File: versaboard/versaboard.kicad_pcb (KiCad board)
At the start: 4 copper layers, 61 x 43 mm, 30 parts, among them J1 UART, J39 Conn_02x20_Odd_Even, J4 DBG, J40 Conn_02x20_Odd_Even, SW1 RST, U1 ATSAML21G18B-AUT, X1 32.768kHz

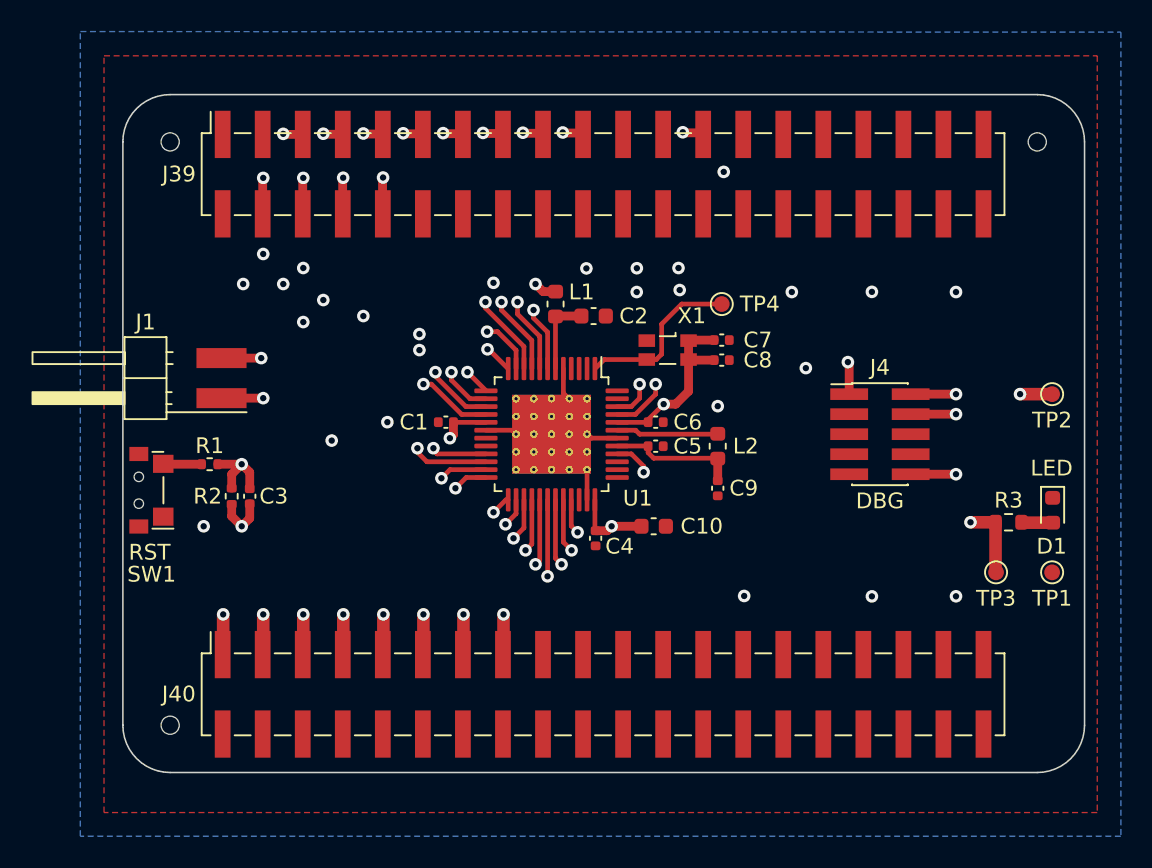
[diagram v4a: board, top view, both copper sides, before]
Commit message: versaboard r0003: avoid FPGA pin bank 1
Pin bank 1 on the ECP5 evaluation board is +2.5V by default and this can
only be changed by resoldering SMD resistors. Yeah, no.
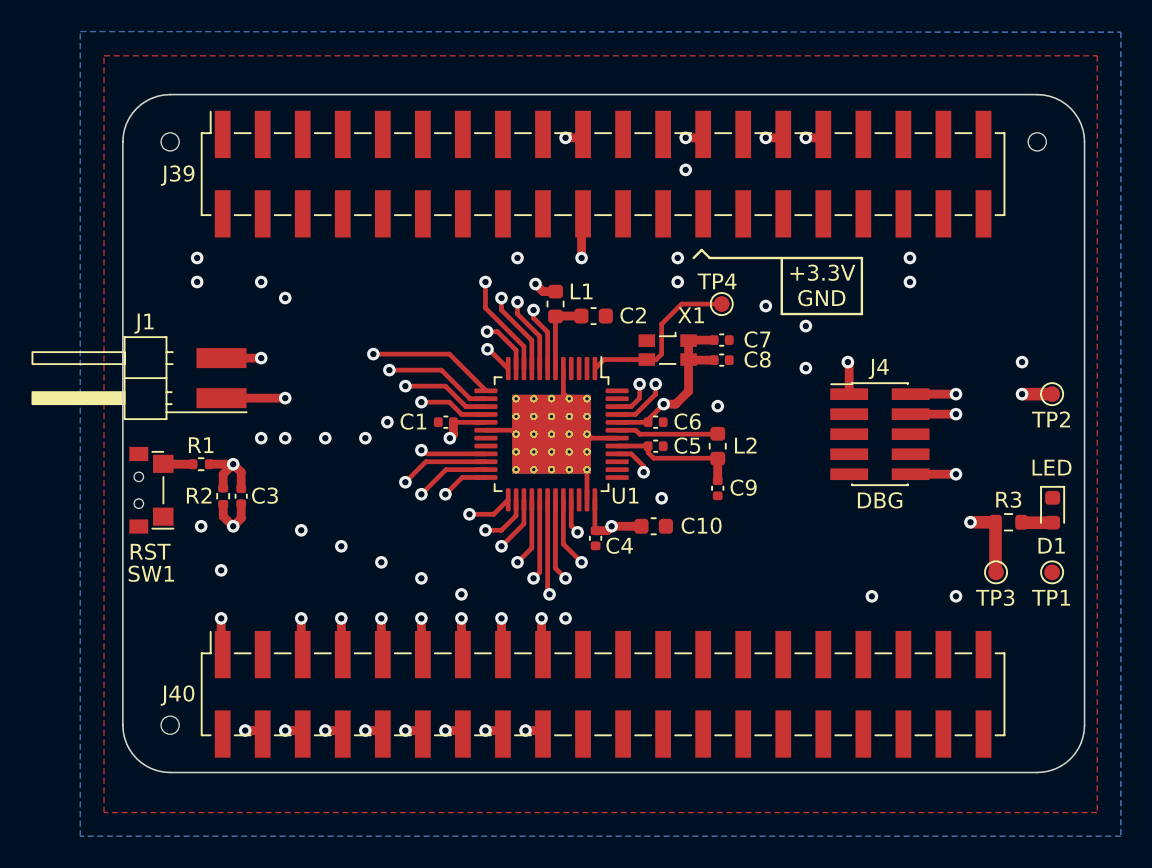
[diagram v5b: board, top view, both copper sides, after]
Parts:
- moved R2 0.54 mm to (36.9, 66.2)
- moved C3 0.54 mm to (38.0, 66.2)
- moved R1 0.54 mm to (35.5, 64.1)
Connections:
- J39 pad 10: /YT -> unconnected-(J39-Pad10)
- J39 pad 11: /NHB3 -> unconnected-(J39-Pad11)
- J39 pad 13: /NHB4 -> unconnected-(J39-Pad13)
- J39 pad 15: /NHB5 -> unconnected-(J39-Pad15)
- J39 pad 17: /NHB6 -> unconnected-(J39-Pad17)
- J39 pad 19: /NHB7 -> /SHB
- J39 pad 20: unconnected-(J39-Pad20) -> /GO
- J39 pad 29: unconnected-(J39-Pad29) -> /MF
- J39 pad 31: unconnected-(J39-Pad31) -> /YT
- J39 pad 4: /SHB -> unconnected-(J39-Pad4)
- J39 pad 5: /NHB0 -> unconnected-(J39-Pad5)
- J39 pad 6: /GO -> unconnected-(J39-Pad6)
- J39 pad 7: /NHB1 -> unconnected-(J39-Pad7)
- J39 pad 8: /MF -> unconnected-(J39-Pad8)
- J39 pad 9: /NHB2 -> unconnected-(J39-Pad9)
- J40 pad 10: unconnected-(J40-Pad10) -> /NHB3
- J40 pad 11: /PB5 -> /PB4
- J40 pad 12: unconnected-(J40-Pad12) -> /NHB4
- J40 pad 13: /PB6 -> /PB5
- J40 pad 14: unconnected-(J40-Pad14) -> /NHB5
- J40 pad 15: /PB7 -> /PB6
- J40 pad 16: unconnected-(J40-Pad16) -> /NHB6
- J40 pad 17: unconnected-(J40-Pad17) -> /PB7
- J40 pad 18: unconnected-(J40-Pad18) -> /NHB7
- J40 pad 3: /PB1 -> unconnected-(J40-Pad3)
- J40 pad 4: unconnected-(J40-Pad4) -> /NHB0
- J40 pad 5: /PB2 -> /PB1
- J40 pad 6: unconnected-(J40-Pad6) -> /NHB1
- J40 pad 7: /PB3 -> /PB2
- J40 pad 8: unconnected-(J40-Pad8) -> /NHB2
- J40 pad 9: /PB4 -> /PB3
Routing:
- net /NHB7: track 62.7 -> 21.1 mm, vias 3 -> 2
- net /NHB6: track 57.0 -> 22.4 mm, vias 3 -> 2
- net /NHB4: track 52.4 -> 25.1 mm
- net /SHB: track 34.7 -> 17.3 mm, vias 3 -> 2
- net /GO: track 28.0 -> 14.7 mm
- net /NHB5: track 34.2 -> 23.5 mm
- net /NHB0: track 28.9 -> 37.4 mm
- net /NHB1: track 27.2 -> 34.8 mm
- net /NHB2: track 24.5 -> 31.7 mm
- net /NHB3: track 22.4 -> 29.2 mm, vias 2 -> 3
- net /RX: track 23.5 -> 28.1 mm
- net /MF: track 37.9 -> 33.5 mm, vias 2 -> 3
- net /YT: track 39.7 -> 35.6 mm, vias 2 -> 3
- net /TX: track 25.6 -> 29.4 mm
- net /PB3: track 20.8 -> 18.6 mm, vias 2 -> 3
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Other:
- board text added: "+3.3V GND"
- board text added: "ntcrackfpga versaboard r0003"
- board text removed: "ntcrackfpga versaboard r0002"

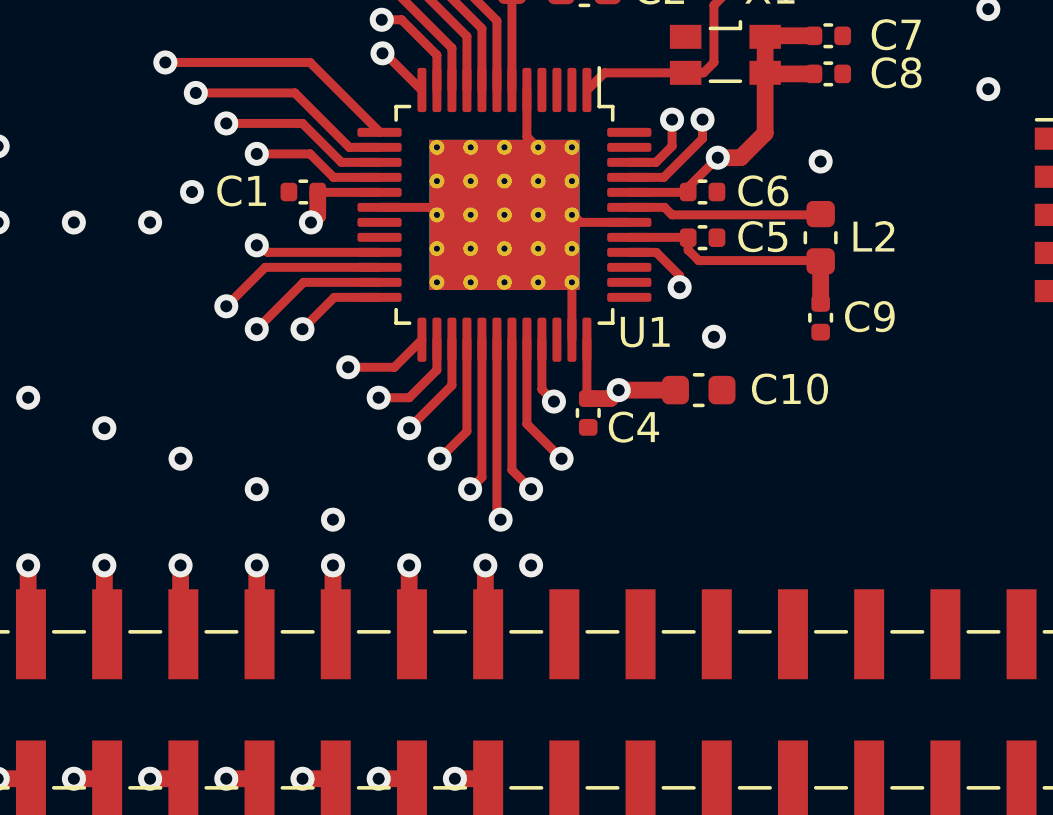
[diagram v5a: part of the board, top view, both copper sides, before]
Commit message: versaboard: add STA, STC and SG pins
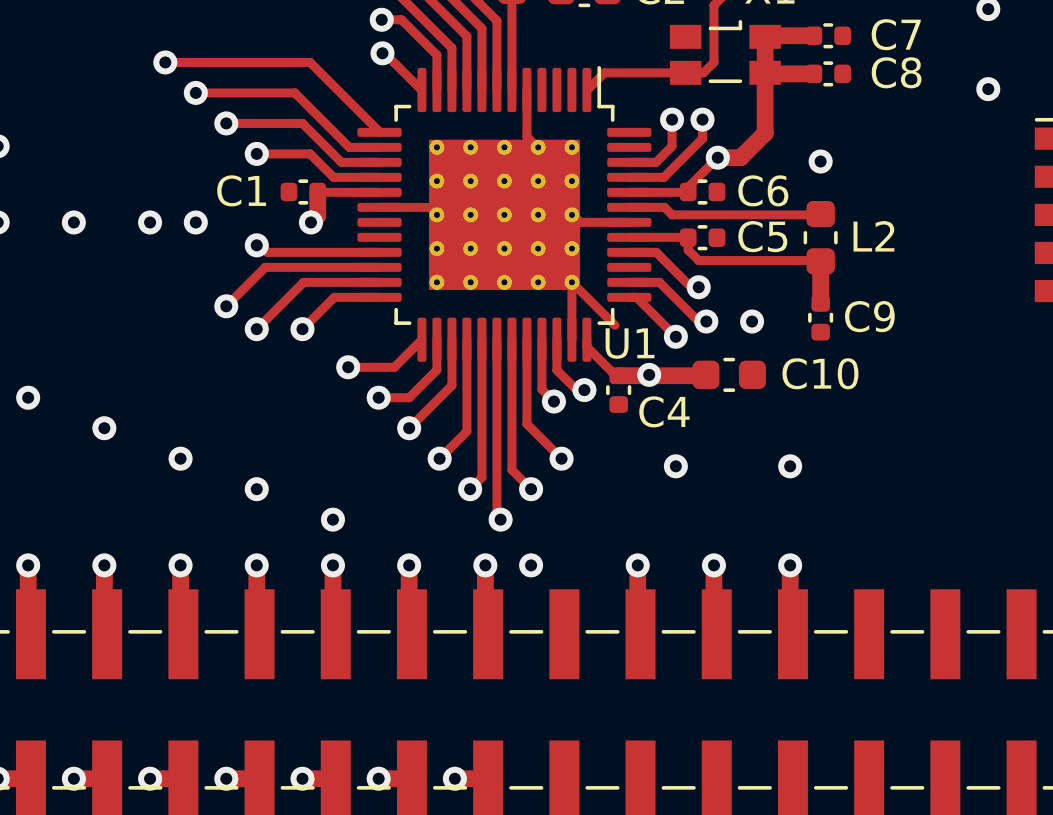
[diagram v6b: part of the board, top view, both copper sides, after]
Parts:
- moved C4 1.27 mm to (61.5, 68.1)
- moved C10 1.14 mm to (65.2, 67.6)
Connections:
- J40 pad 21: unconnected-(J40-Pad21) -> /STA
- J40 pad 23: unconnected-(J40-Pad23) -> /STC
- J40 pad 25: unconnected-(J40-Pad25) -> /SG
- U1 pad 3: unconnected-(U1-Pad3) -> GND
- U1 pad 34: unconnected-(U1-Pad34) -> /STA
- U1 pad 37: unconnected-(U1-Pad37) -> /SG
- U1 pad 38: unconnected-(U1-Pad38) -> /STC
- U1 pad 4: unconnected-(U1-Pad4) -> GND
- U1 pad 47: unconnected-(U1-Pad47) -> GND
- U1 pad 48: unconnected-(U1-Pad48) -> GND
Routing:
- net /SG: track 0.00 -> 15.1 mm, vias 0 -> 4
- net /STC: track 0.00 -> 13.4 mm, vias 0 -> 2
- net /STA: track 0.00 -> 10.8 mm, vias 0 -> 2
- net GND: track 7.93 -> 9.96 mm
- net +3.3V: track 29.5 -> 29.0 mm

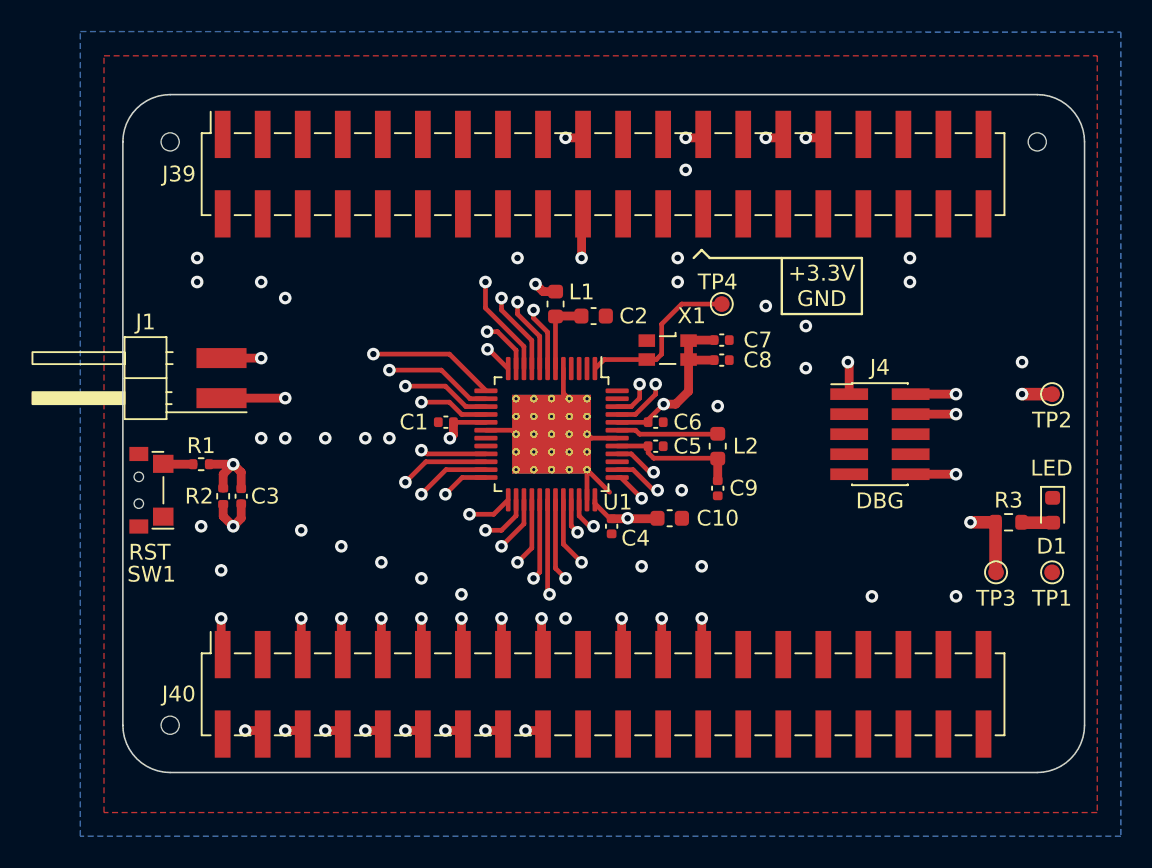
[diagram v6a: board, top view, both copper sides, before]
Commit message: versaboard: lead more pins to J40 for potential future use
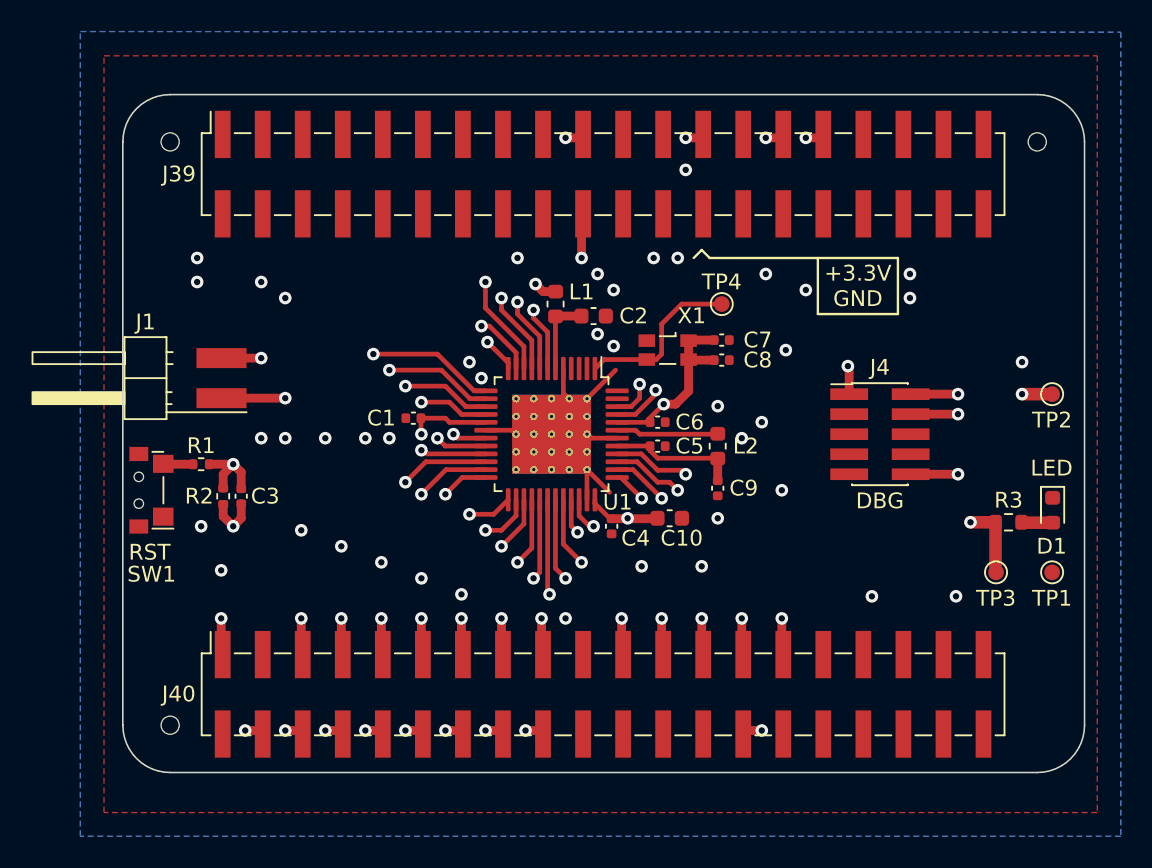
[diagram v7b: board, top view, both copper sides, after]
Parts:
- moved C1 2.08 mm to (48.9, 61.2)
- moved C5 0.13 mm to (64.4, 63.0)
- moved C6 0.13 mm to (64.4, 61.5)
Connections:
- net /PB0 renamed /OB0
- net /PB1 renamed /OB1
- net /PB2 renamed /OB2
- net /PB3 renamed /OB3
- net /PB4 renamed /OB4
- net /PB5 renamed /OB5
- net /PB6 renamed /OB6
- net /PB7 renamed /OB7
- J40 pad 27: unconnected-(J40-Pad27) -> /FFU0
- J40 pad 28: unconnected-(J40-Pad28) -> /FFU1
- J40 pad 29: unconnected-(J40-Pad29) -> /FFU2
- U1 pad 19: unconnected-(U1-Pad19) -> /FFU0
- U1 pad 20: unconnected-(U1-Pad20) -> /FFU1
- U1 pad 39: unconnected-(U1-Pad39) -> /FFU2
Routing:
- net /FFU1: track 0.00 -> 49.6 mm, vias 0 -> 4
- net /FFU0: track 0.00 -> 38.3 mm, vias 0 -> 4
- net /FFU2: track 0.00 -> 20.6 mm, vias 0 -> 3
- net /~{RST}: track 57.0 -> 59.8 mm
- net GND: track 9.96 -> 12.5 mm
- net /SWDIO: track 28.4 -> 26.4 mm
- net +3.3V: track 29.0 -> 30.9 mm
- net /MF: track 33.5 -> 35.3 mm, vias 3 -> 5
- net /YT: track 35.6 -> 37.0 mm, vias 3 -> 5
- net /SWCLK: track 26.3 -> 25.7 mm
